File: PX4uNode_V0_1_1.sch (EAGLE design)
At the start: 140 parts, among them M3_MOUNT1101 MOUNT-HOLE3.1MM, M3_MOUNT1102 MOUNT-HOLE3.1MM, M3_MOUNT1103 MOUNT-HOLE3.1MM, M3_MOUNT1104 MOUNT-HOLE3.1MM, U101 STM32F4X7VX, U401 MAX3051, U402 MAX3051, X1 USB-MICROB, X101 3.2x2.5 mm / 24 MHz / 15 ppm

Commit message: uNode - Bit more layout
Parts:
- removed JP4: (no value), SparkFun-Connectors:M07
- removed X1: USB-MICROB, pixhawk2:USB-MICROB
- added U$1: M04X2, SparkFun-Connectors:M04X2
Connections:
- net !SPI_EXT_NSS: now also U$1.3; no longer JP4.5
- net GND: now also U$1.7; no longer JP4.7, X1.GND
- net GPIO_EXT_1: now also U$1.5; no longer JP4.6
- net N$41: now also U$1.8; no longer JP4.1
- net OTG_DM1: no longer X1.D-
- net OTG_DP1: no longer X1.D+
- net SPI_EXT_MISO: now also U$1.2; no longer JP4.3
- net SPI_EXT_MOSI: now also U$1.1; no longer JP4.4
- net SPI_EXT_SCK: now also U$1.4; no longer JP4.2
- net VBUS: no longer X1.VBUS
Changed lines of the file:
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@@
 <attribute name="BOM" value="EXCLUDE"/>
 </part>
-<part name="JP4" library="SparkFun-Connectors" deviceset="M07" device=""/>
 <part name="JP5" library="SparkFun-Connectors" deviceset="M04" device="PTH"/>
 <part name="JP6" library="SparkFun-Connectors" deviceset="M04" device="PTH"/>
@@
 <part name="JP9" library="SparkFun-Connectors" deviceset="M03" device="PTH"/>
 <part name="JP10" library="SparkFun-Connectors" deviceset="M03" device="PTH"/>
-<part name="X1" library="pixhawk2" deviceset="USB" device="-MICROB"/>
 <part name="JP11" library="SparkFun-Connectors" deviceset="M04" device="PTH"/>
 <part name="JP12" library="SparkFun-Connectors" deviceset="M03X2" device="2X3_SILK_SM"/>
@@
 <part name="D1" library="SparkFun-DiscreteSemi" deviceset="DIODE-SCHOTTKY" device=""/>
 <part name="D2" library="SparkFun-DiscreteSemi" deviceset="DIODE-SCHOTTKY" device=""/>
+<part name="U$1" library="SparkFun-Connectors" deviceset="M04X2" device=""/>
 </parts>
 <sheets>
@@
 <attribute name="PARTNO" x="58.42" y="50.8" size="1.778" layer="96" display="off"/>
 </instance>
-<instance part="X1" gate="G$1" x="88.9" y="142.24"/>
 <instance part="JP11" gate="G$1" x="91.44" y="132.08" rot="R180"/>
 </instances>
@@
 <wire x1="73.66" y1="139.7" x2="66.04" y2="139.7" width="0.1524" layer="91"/>
 <pinref part="U$301" gate="G$1" pin="D2I"/>
-<wire x1="73.66" y1="139.7" x2="73.66" y2="147.32" width="0.1524" layer="91"/>
-<pinref part="X1" gate="G$1" pin="D-"/>
-<wire x1="73.66" y1="147.32" x2="86.36" y2="147.32" width="0.1524" layer="91"/>
 <pinref part="JP11" gate="G$1" pin="3"/>
 </segment>
@@
 <pinref part="U$301" gate="G$1" pin="D1I"/>
 <wire x1="71.12" y1="132.08" x2="86.36" y2="132.08" width="0.1524" layer="91"/>
-<pinref part="X1" gate="G$1" pin="D+"/>
-<wire x1="86.36" y1="149.86" x2="71.12" y2="149.86" width="0.1524" layer="91"/>
-<wire x1="71.12" y1="149.86" x2="71.12" y2="132.08" width="0.1524" layer="91"/>
 <pinref part="JP11" gate="G$1" pin="2"/>
 </segment>
@@
 <pinref part="U$301" gate="G$1" pin="GND"/>
 <wire x1="81.28" y1="127" x2="86.36" y2="127" width="0.1524" layer="91"/>
-<pinref part="X1" gate="G$1" pin="GND"/>
-<wire x1="86.36" y1="142.24" x2="81.28" y2="142.24" width="0.1524" layer="91"/>
-<wire x1="81.28" y1="142.24" x2="81.28" y2="127" width="0.1524" layer="91"/>
 <pinref part="JP11" gate="G$1" pin="4"/>
 </segment>
@@
 <label x="50.8" y="162.56" size="1.27" layer="95" rot="R180" xref="yes"/>
 <wire x1="78.74" y1="162.56" x2="50.8" y2="162.56" width="0.1524" layer="91"/>
-<wire x1="78.74" y1="162.56" x2="78.74" y2="144.78" width="0.1524" layer="91"/>
-<wire x1="78.74" y1="144.78" x2="78.74" y2="134.62" width="0.1524" layer="91"/>
+<wire x1="78.74" y1="162.56" x2="78.74" y2="134.62" width="0.1524" layer="91"/>
 <wire x1="78.74" y1="134.62" x2="86.36" y2="134.62" width="0.1524" layer="91"/>
-<pinref part="X1" gate="G$1" pin="VBUS"/>
-<wire x1="86.36" y1="144.78" x2="78.74" y2="144.78" width="0.1524" layer="91"/>
 <pinref part="JP11" gate="G$1" pin="1"/>
 </segment>
@@
 <instances>
 <instance part="FRAME9" gate="G$1" x="0" y="0"/>
-<instance part="GND70" gate="1" x="88.9" y="134.62"/>
+<instance part="GND70" gate="1" x="60.96" y="132.08"/>
 <instance part="L401" gate="G$1" x="60.96" y="160.02">
 <attribute name="PARTNO" x="60.96" y="160.02" size="1.778" layer="96" display="off"/>
@@
 <attribute name="BOM" x="134.62" y="114.3" size="1.778" layer="96" display="off"/>
 </instance>
-<instance part="JP4" gate="G$1" x="93.98" y="149.86" rot="R180"/>
 <instance part="JP5" gate="G$1" x="99.06" y="83.82" rot="R180"/>
 <instance part="JP6" gate="G$1" x="99.06" y="20.32" rot="R180"/>
@@
 <instance part="JP8" gate="G$1" x="241.3" y="101.6" rot="R180"/>
 <instance part="JP9" gate="G$1" x="228.6" y="160.02" rot="R180"/>
+<instance part="U$1" gate="G$1" x="78.74" y="142.24"/>
 </instances>
 <busses>
@@
 <wire x1="88.9" y1="149.86" x2="48.26" y2="149.86" width="0.1524" layer="91"/>
 <label x="48.26" y="149.86" size="1.27" layer="95" rot="R180" xref="yes"/>
-<pinref part="JP4" gate="G$1" pin="3"/>
+<wire x1="88.9" y1="149.86" x2="88.9" y2="147.32" width="0.1524" layer="91"/>
+<pinref part="U$1" gate="G$1" pin="2"/>
+<wire x1="88.9" y1="147.32" x2="86.36" y2="147.32" width="0.1524" layer="91"/>
 </segment>
 </net>
 <net name="SPI_EXT_MOSI" class="0">
 <segment>
-<wire x1="88.9" y1="147.32" x2="48.26" y2="147.32" width="0.1524" layer="91"/>
+<wire x1="71.12" y1="147.32" x2="48.26" y2="147.32" width="0.1524" layer="91"/>
 <label x="48.26" y="147.32" size="1.27" layer="95" rot="R180" xref="yes"/>
-<pinref part="JP4" gate="G$1" pin="4"/>
+<pinref part="U$1" gate="G$1" pin="1"/>
 </segment>
 </net>
 <net name="SPI_EXT_SCK" class="0">
 <segment>
-<wire x1="88.9" y1="152.4" x2="48.26" y2="152.4" width="0.1524" layer="91"/>
+<wire x1="91.44" y1="152.4" x2="48.26" y2="152.4" width="0.1524" layer="91"/>
 <label x="48.26" y="152.4" size="1.27" layer="95" rot="R180" xref="yes"/>
-<pinref part="JP4" gate="G$1" pin="2"/>
+<wire x1="91.44" y1="152.4" x2="91.44" y2="144.78" width="0.1524" layer="91"/>
+<pinref part="U$1" gate="G$1" pin="4"/>
+<wire x1="91.44" y1="144.78" x2="86.36" y2="144.78" width="0.1524" layer="91"/>
 </segment>
 </net>
 <net name="!SPI_EXT_NSS" class="0">
 <segment>
-<wire x1="88.9" y1="144.78" x2="48.26" y2="144.78" width="0.1524" layer="91"/>
+<wire x1="71.12" y1="144.78" x2="48.26" y2="144.78" width="0.1524" layer="91"/>
 <label x="48.26" y="144.78" size="1.27" layer="95" rot="R180" xref="yes"/>
-<pinref part="JP4" gate="G$1" pin="5"/>
+<pinref part="U$1" gate="G$1" pin="3"/>
 </segment>
 </net>
 <net name="N$41" class="1">
 <segment>
-<wire x1="88.9" y1="154.94" x2="86.36" y2="154.94" width="0.1524" layer="91"/>
-<wire x1="86.36" y1="154.94" x2="86.36" y2="160.02" width="0.1524" layer="91"/>
 <pinref part="L401" gate="G$1" pin="P$2"/>
-<wire x1="86.36" y1="160.02" x2="66.04" y2="160.02" width="0.1524" layer="91"/>
-<pinref part="JP4" gate="G$1" pin="1"/>
+<wire x1="93.98" y1="160.02" x2="66.04" y2="160.02" width="0.1524" layer="91"/>
+<wire x1="93.98" y1="160.02" x2="93.98" y2="139.7" width="0.1524" layer="91"/>
+<pinref part="U$1" gate="G$1" pin="8"/>
+<wire x1="93.98" y1="139.7" x2="86.36" y2="139.7" width="0.1524" layer="91"/>
 </segment>
 </net>
@@
 <net name="GPIO_EXT_1" class="0">
 <segment>
-<wire x1="88.9" y1="142.24" x2="48.26" y2="142.24" width="0.1524" layer="91"/>
+<wire x1="71.12" y1="142.24" x2="48.26" y2="142.24" width="0.1524" layer="91"/>
 <label x="48.26" y="142.24" size="1.27" layer="95" rot="R180" xref="yes"/>
-<pinref part="JP4" gate="G$1" pin="6"/>
+<pinref part="U$1" gate="G$1" pin="5"/>
 </segment>
 </net>
@@
 </segment>
 <segment>
-<wire x1="88.9" y1="139.7" x2="88.9" y2="137.16" width="0.1524" layer="91"/>
 <pinref part="GND70" gate="1" pin="GND"/>
-<wire x1="88.9" y1="139.7" x2="81.28" y2="139.7" width="0.1524" layer="91"/>
 <pinref part="L401" gate="G$1" pin="P$3"/>
-<wire x1="81.28" y1="139.7" x2="60.96" y2="139.7" width="0.1524" layer="91"/>
+<wire x1="60.96" y1="134.62" x2="60.96" y2="139.7" width="0.1524" layer="91"/>
+<pinref part="U$1" gate="G$1" pin="7"/>
 <wire x1="60.96" y1="139.7" x2="60.96" y2="154.94" width="0.1524" layer="91"/>
-<wire x1="81.28" y1="154.94" x2="81.28" y2="139.7" width="0.1524" layer="91"/>
-<junction x="81.28" y="139.7"/>
-<pinref part="JP4" gate="G$1" pin="7"/>
-<junction x="88.9" y="139.7"/>
-</segment>
-<segment>
+<wire x1="71.12" y1="139.7" x2="60.96" y2="139.7" width="0.1524" layer="91"/>
+<junction x="60.96" y="139.7"/>
+</segment>
+<segment>

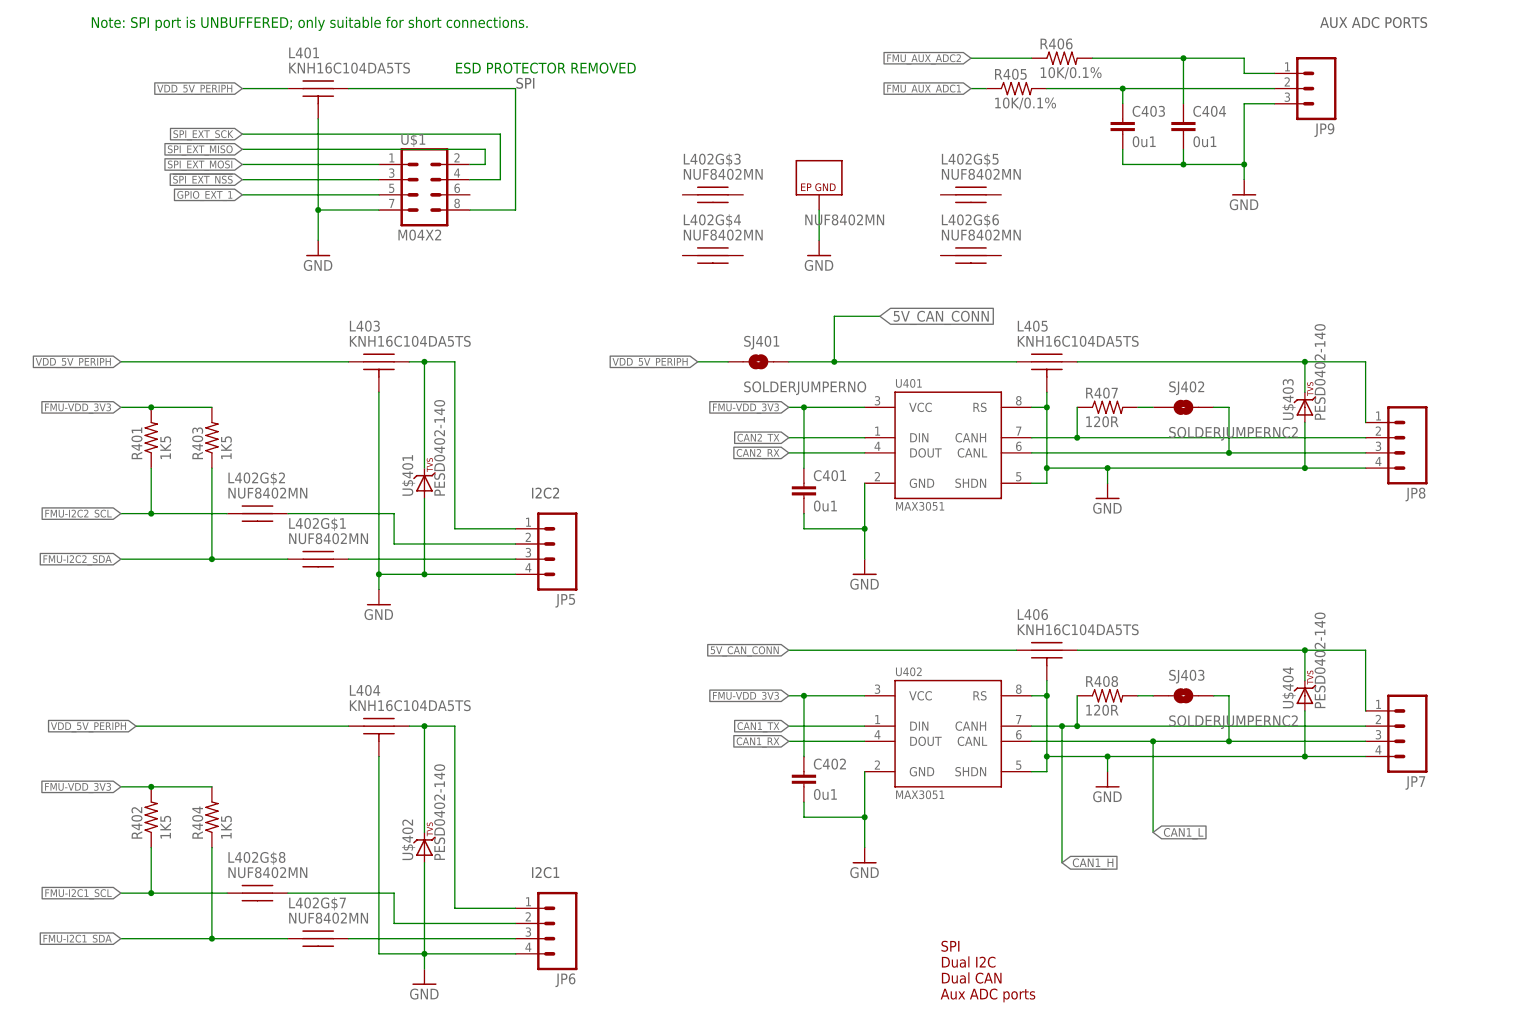
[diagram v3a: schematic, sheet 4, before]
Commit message: CAN layout done
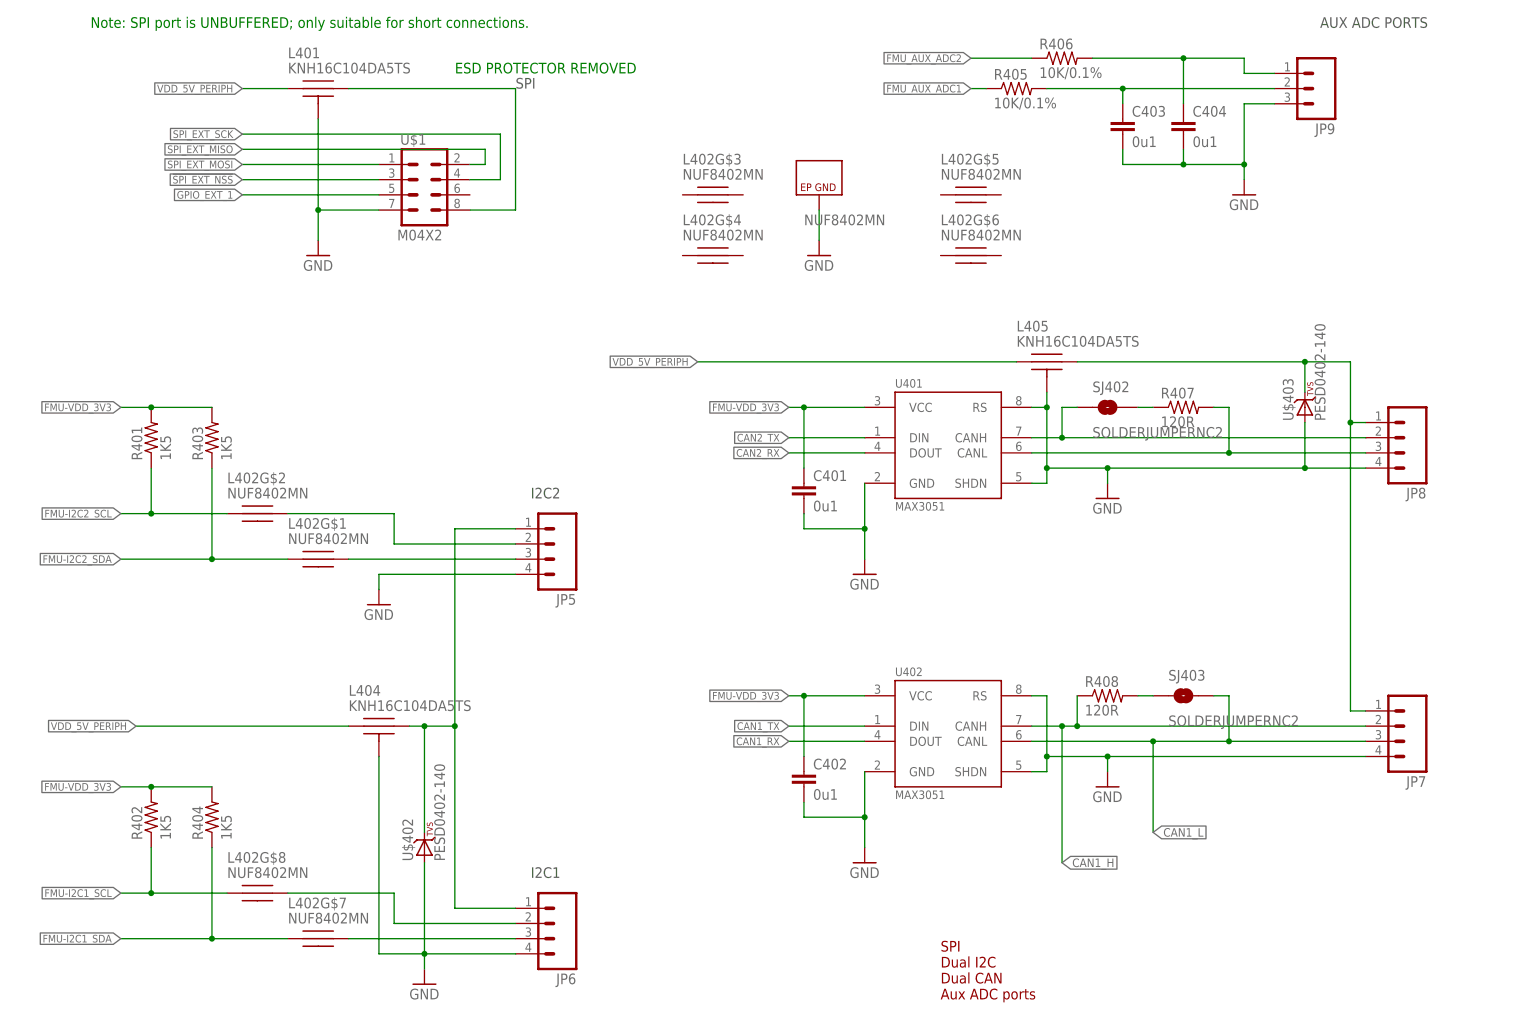
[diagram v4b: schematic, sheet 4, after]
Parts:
- removed L403, L406: KNH16C104DA5TS, PX4lite:KNH16C104DA5TS
- removed SJ401: SOLDERJUMPERNO, SparkFun-Passives:SOLDERJUMPERNO
- removed U$401, U$404: PESD0402-140, pixhawk2:DIODE-TVS
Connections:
- removed net 5V_CAN_CONN: L405.P$1, L406.P$1, SJ401.2
- removed net N$29: R407.2, SJ402.1
- removed net N$42: JP6.1, L404.P$2, U$402.C
- removed net N$48: JP7.1, L406.P$2, U$404.C
- new net IC2_VDD_5V: JP5.1, JP6.1, L404.P$2, U$402.C
- net CAN2_H: now also SJ402.1; no longer R407.1
- net CAN2_L: now also R407.2; no longer SJ402.2
- net GND: no longer L403.P$3, L406.P$3, U$401.A, U$404.A
- net N$21: now also R407.1, SJ402.2; no longer JP5.1, L403.P$2, U$401.C
- net N$28: now also JP7.1
- net VDD_5V_PERIPH: now also L405.P$1; no longer L403.P$1, SJ401.1
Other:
- moved on the sheet: R407, SJ402

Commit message: uNode - More layout
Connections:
- net N$1 renamed CLK2
- net N$12 renamed VCAP_1
- net N$2 renamed CLK1
- net N$8 renamed VCAP_2
- net OTG_DM1 renamed UDB_DP
- net OTG_DP1 renamed USB_DM
- net FMU-CH3: now also L1001G$5.P$1; no longer L1001G$6.P$1
- net FMU-CH4: now also L1001G$6.P$1; no longer L1001G$5.P$1
- net N$77: now also L1001G$6.P$2; no longer L1001G$5.P$2
- net N$78: now also L1001G$5.P$2; no longer L1001G$6.P$2
- net OTG_FS_DM: now also U$301.D1O; no longer U$301.D2O
- net OTG_FS_DP: now also U$301.D2O; no longer U$301.D1O
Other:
- moved on the sheet: L1001G$5, L1001G$6
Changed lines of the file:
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@@
 </segment>
 </net>
-<net name="N$1" class="0">
+<net name="CLK2" class="0">
 <segment>
 <wire x1="175.26" y1="88.9" x2="190.5" y2="88.9" width="0.1524" layer="91"/>
@@
 </segment>
 </net>
-<net name="N$2" class="0">
+<net name="CLK1" class="0">
 <segment>
 <wire x1="175.26" y1="93.98" x2="180.34" y2="93.98" width="0.1524" layer="91"/>
@@
 </segment>
 </net>
-<net name="OTG_DM1" class="0">
-<segment>
-<wire x1="86.36" y1="129.54" x2="73.66" y2="129.54" width="0.1524" layer="91"/>
-<wire x1="73.66" y1="129.54" x2="73.66" y2="139.7" width="0.1524" layer="91"/>
-<wire x1="73.66" y1="139.7" x2="66.04" y2="139.7" width="0.1524" layer="91"/>
-<pinref part="U$301" gate="G$1" pin="D2I"/>
-<pinref part="JP11" gate="G$1" pin="3"/>
-</segment>
-</net>
-<net name="OTG_DP1" class="0">
-<segment>
-<wire x1="71.12" y1="132.08" x2="71.12" y2="129.54" width="0.1524" layer="91"/>
-<wire x1="66.04" y1="129.54" x2="71.12" y2="129.54" width="0.1524" layer="91"/>
-<pinref part="U$301" gate="G$1" pin="D1I"/>
-<wire x1="71.12" y1="132.08" x2="86.36" y2="132.08" width="0.1524" layer="91"/>
-<pinref part="JP11" gate="G$1" pin="2"/>
-</segment>
-</net>
 <net name="OTG_FS_DP" class="0">
 <segment>
-<wire x1="40.64" y1="129.54" x2="33.02" y2="129.54" width="0.1524" layer="91"/>
-<label x="33.02" y="129.54" size="1.27" layer="95" font="vector" rot="R180" xref="yes"/>
-<pinref part="U$301" gate="G$1" pin="D1O"/>
-</segment>
-</net>
-<net name="OTG_FS_DM" class="0">
-<segment>
 <wire x1="40.64" y1="139.7" x2="33.02" y2="139.7" width="0.1524" layer="91"/>
 <label x="33.02" y="139.7" size="1.27" layer="95" font="vector" rot="R180" xref="yes"/>
@@
 </segment>
 </net>
+<net name="OTG_FS_DM" class="0">
+<segment>
+<wire x1="40.64" y1="129.54" x2="33.02" y2="129.54" width="0.1524" layer="91"/>
+<label x="33.02" y="129.54" size="1.27" layer="95" font="vector" rot="R180" xref="yes"/>
+<pinref part="U$301" gate="G$1" pin="D1O"/>
+</segment>
+</net>
+<net name="UDB_DP" class="0">
+<segment>
+<pinref part="U$301" gate="G$1" pin="D2I"/>
+<wire x1="66.04" y1="139.7" x2="73.66" y2="139.7" width="0.1524" layer="91"/>
+<wire x1="73.66" y1="139.7" x2="73.66" y2="129.54" width="0.1524" layer="91"/>
+<pinref part="JP11" gate="G$1" pin="3"/>
+<wire x1="73.66" y1="129.54" x2="86.36" y2="129.54" width="0.1524" layer="91"/>
+</segment>
+</net>
+<net name="USB_DM" class="0">
+<segment>
+<pinref part="JP11" gate="G$1" pin="2"/>
+<wire x1="86.36" y1="132.08" x2="71.12" y2="132.08" width="0.1524" layer="91"/>
+<wire x1="71.12" y1="132.08" x2="71.12" y2="129.54" width="0.1524" layer="91"/>
+<pinref part="U$301" gate="G$1" pin="D1I"/>
+<wire x1="71.12" y1="129.54" x2="66.04" y2="129.54" width="0.1524" layer="91"/>
+</segment>
+</net>
 </nets>
 </sheet>
@@
 </segment>
 </net>
-<net name="N$8" class="0">
+<net name="VCAP_2" class="0">
 <segment>
 <pinref part="U101" gate="G$2" pin="VCAP_2"/>
@@
 </segment>
 </net>
-<net name="N$12" class="0">
+<net name="VCAP_1" class="0">
 <segment>
 <pinref part="U101" gate="G$2" pin="VCAP_1"/>
@@
 <instance part="L1001" gate="G$8" x="81.28" y="99.06"/>
 <instance part="L1001" gate="G$7" x="68.58" y="104.14"/>
-<instance part="L1001" gate="G$6" x="53.34" y="109.22"/>
-<instance part="L1001" gate="G$5" x="81.28" y="114.3"/>
+<instance part="L1001" gate="G$5" x="53.34" y="109.22"/>
+<instance part="L1001" gate="G$6" x="81.28" y="114.3"/>
 <instance part="L1001" gate="G$4" x="66.04" y="119.38"/>
 <instance part="L1001" gate="G$3" x="53.34" y="124.46"/>
@@
 <wire x1="40.64" y1="109.22" x2="48.26" y2="109.22" width="0.1524" layer="91"/>
 <label x="40.64" y="109.22" size="1.27" layer="95" rot="R180" xref="yes"/>
-<pinref part="L1001" gate="G$6" pin="P$1"/>
+<pinref part="L1001" gate="G$5" pin="P$1"/>
 </segment>
 </net>
@@
 <net name="N$77" class="0">
 <segment>
-<pinref part="L1001" gate="G$5" pin="P$2"/>
+<pinref part="L1001" gate="G$6" pin="P$2"/>
 <wire x1="86.36" y1="114.3" x2="99.06" y2="114.3" width="0.1524" layer="91"/>
 <pinref part="J1001" gate="-CH4" pin="S"/>
@@
 <net name="N$78" class="0">
 <segment>
-<pinref part="L1001" gate="G$6" pin="P$2"/>
+<pinref part="L1001" gate="G$5" pin="P$2"/>
 <wire x1="58.42" y1="109.22" x2="99.06" y2="109.22" width="0.1524" layer="91"/>
 <pinref part="J1001" gate="-CH3" pin="S"/>
@@
 <wire x1="40.64" y1="114.3" x2="76.2" y2="114.3" width="0.1524" layer="91"/>
 <label x="40.64" y="114.3" size="1.27" layer="95" rot="R180" xref="yes"/>
-<pinref part="L1001" gate="G$5" pin="P$1"/>
+<pinref part="L1001" gate="G$6" pin="P$1"/>
 </segment>
 </net>

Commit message: uNode - Just more layout
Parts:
- removed L203, L204: KNH16C104DA5TS, PX4lite:KNH16C104DA5TS
- removed U$203, U$204: PESD0402-140, pixhawk2:DIODE-TVS
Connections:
- removed net 5V_S1_FILTERED: JP12.2, L203.P$2, U$203.C
- removed net 5V_S2_FILTERED: JP1.2, L204.P$2, U$204.C
- net !SPI_EXT_NSS: now also U$1.4; no longer U$1.3
- net 5V_S3_FILTERED: now also JP1.2, JP12.2
- net FMU-I2C1_SCL: now also L402G$2.P$1; no longer L402G$8.P$1
- net FMU-I2C2_SCL: now also L402G$4.P$1; no longer L402G$2.P$1
- net FMU-I2C2_SDA: now also L402G$8.P$1; no longer L402G$1.P$1
- net GND: no longer L203.P$3, L204.P$3, U$203.A, U$204.A
- net N$20: now also L402G$8.P$2; no longer L402G$1.P$2
- net N$33: now also L402G$2.P$2; no longer L402G$8.P$2
- net N$4: now also L402G$4.P$2; no longer L402G$2.P$2
- net SPI_EXT_MISO: now also U$1.3; no longer U$1.2
- net SPI_EXT_MOSI: now also U$1.6; no longer U$1.1
- net SPI_EXT_SCK: now also U$1.2; no longer U$1.4
- net VDD_5V_PERIPH: no longer L203.P$1, L204.P$1
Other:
- moved on the sheet: L402G$1, L402G$2, L402G$4, L402G$8, U$205
